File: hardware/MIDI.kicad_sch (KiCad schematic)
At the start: 0 parts

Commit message: feat: Created DIN5 MIDI Interface to Schematic
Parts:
- added D1, D3: LED, symbol Device:LED
- added D2: 1N4148, Diode_THT:D_DO-35_SOD27_P7.62mm_Horizontal, symbol Diode:1N4148
- added J2: DIN5_OUT, symbol Connector:DIN-5
- added J3: DIN5_IN, symbol Connector:DIN-5
- added R10, R11, R6, R7, R8, R9: R_US, symbol Device:R_US
- added U2: H11L1, symbol Isolator:H11L1
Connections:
- new net: D3.2 (A), R11.2
- new net: D2.1 (K), R10.2, U2.1
- new net: D2.2 (A), J3.5, U2.2
- new net: D1.2 (A), R8.2
- new net: J3.4, R10.1
- new net: J2.4, R9.2
- new net: J2.5, R7.1
- new net +5V: R11.1, R6.1, R8.1, R9.1, U2.6
- new net GND: J2.2, J3.2, U2.5
- new net RX: D3.1 (K), R6.2, U2.4
- new net TX: D1.1 (K), R7.2
- no-connect marks 0 -> 4
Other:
- note added: "Inspired by Adafruit MIDI Featherwing Schematic"

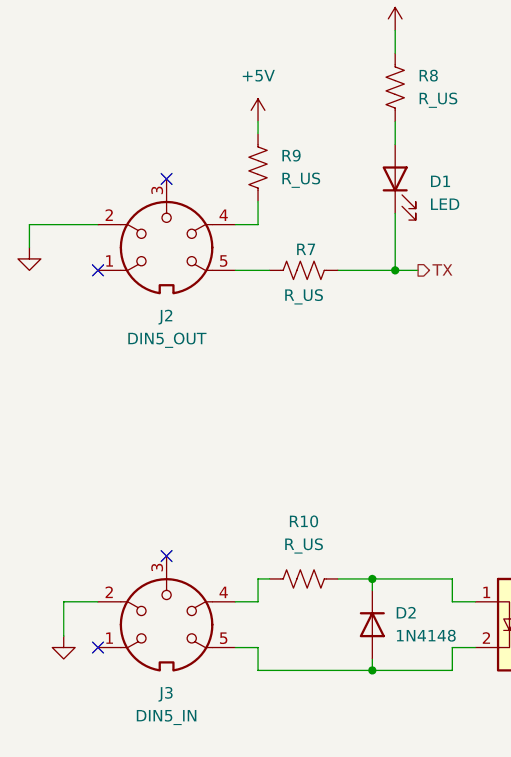
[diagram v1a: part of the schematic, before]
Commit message: feat: Created Button I2C Interfaces
For now, all we are using is generic 1x5 Connectors following the DFR Robot's RGB Button pinout https://wiki.dfrobot.com/SKU_DFR0991_Gravity_I2C_RGB_LED_Button_Module#target_9
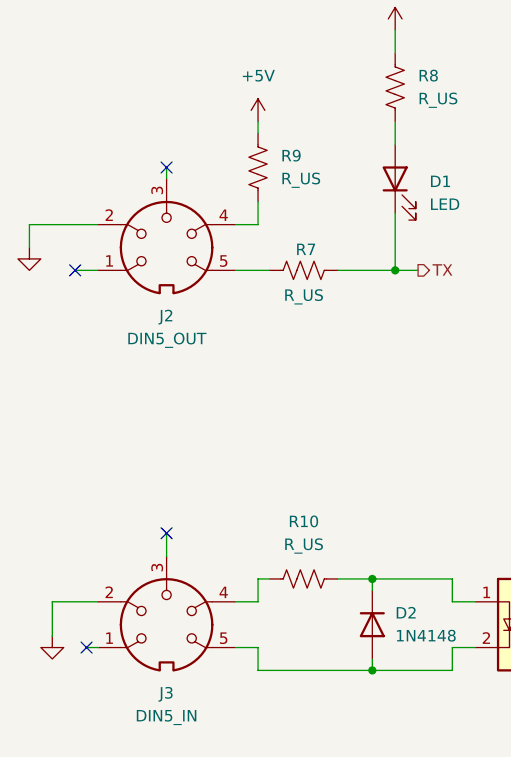
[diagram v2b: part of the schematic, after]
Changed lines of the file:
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@@
 	)
 	(no_connect
-		(at 63.5 52.07)
+		(at 63.5 50.8)
 	)
 	(no_connect
-		(at 55.88 104.14)
+		(at 54.61 104.14)
 	)
 	(no_connect
-		(at 63.5 93.98)
+		(at 63.5 91.44)
 	)
 	(no_connect
-		(at 55.88 62.23)
+		(at 53.34 62.23)
 	)
 	(wire
@@
 	(wire
 		(pts
+			(xy 53.34 62.23) (xy 55.88 62.23)
+		)
+		(stroke
+			(width 0)
+			(type default)
+		)
+	)
+	(wire
+		(pts
 			(xy 134.62 101.6) (xy 139.7 101.6)
 		)
@@
 	(wire
 		(pts
+			(xy 63.5 91.44) (xy 63.5 93.98)
+		)
+		(stroke
+			(width 0)
+			(type default)
+		)
+	)
+	(wire
+		(pts
 			(xy 134.62 76.2) (xy 134.62 78.74)
 		)
@@
 	(wire
 		(pts
-			(xy 52.07 99.06) (xy 55.88 99.06)
+			(xy 50.8 99.06) (xy 55.88 99.06)
 		)
 		(stroke
@@
 	(wire
 		(pts
+			(xy 63.5 50.8) (xy 63.5 52.07)
+		)
+		(stroke
+			(width 0)
+			(type default)
+		)
+	)
+	(wire
+		(pts
 			(xy 95.25 104.14) (xy 97.79 104.14)
 		)
@@
 	(wire
 		(pts
+			(xy 54.61 104.14) (xy 55.88 104.14)
+		)
+		(stroke
+			(width 0)
+			(type default)
+		)
+	)
+	(wire
+		(pts
 			(xy 73.66 96.52) (xy 74.93 96.52)
 		)
@@
 	(wire
 		(pts
-			(xy 52.07 99.06) (xy 52.07 102.87)
+			(xy 50.8 99.06) (xy 50.8 102.87)
 		)
 		(stroke
@@
 	(symbol
 		(lib_id "4ms_Power-symbol:GND")
-		(at 52.07 102.87 0)
+		(at 50.8 102.87 0)
 		(unit 1)
 		(exclude_from_sim no)
@@
 		(fields_autoplaced yes)
 		(property "Reference" "#PWR014"
-			(at 52.07 109.22 0)
+			(at 50.8 109.22 0)
 			(effects
 				(font
@@
 		)
 		(property "Value" "GND"
-			(at 52.07 107.95 0)
+			(at 50.8 107.95 0)
 			(effects
 				(font
@@
 		)
 		(property "Footprint" ""
-			(at 52.07 102.87 0)
+			(at 50.8 102.87 0)
 			(effects
 				(font
@@
 		)
 		(property "Datasheet" ""
-			(at 52.07 102.87 0)
+			(at 50.8 102.87 0)
 			(effects
 				(font
@@
 		)
 		(property "Description" ""
-			(at 52.07 102.87 0)
-			(effects
-				(font
+			(at 50.8 102.87 0)
+			(effects
+				(font

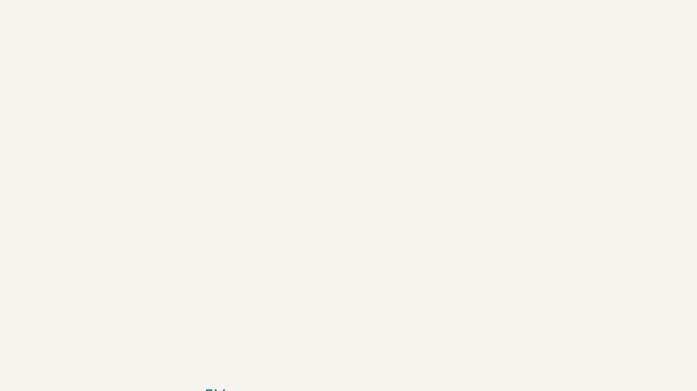
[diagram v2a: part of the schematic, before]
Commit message: feat: Added Footswitch Jack Conn for Tap Tempo
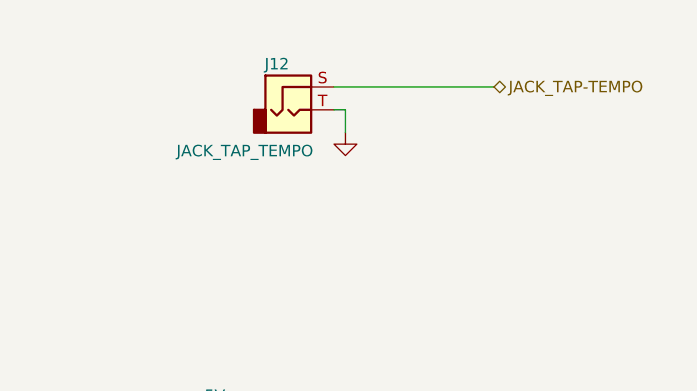
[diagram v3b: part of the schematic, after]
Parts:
- added J12: JACK_TAP_TEMPO, symbol Connector_Audio:AudioJack2
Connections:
- net GND: now also J12.T
- new net JACK_TAP-TEMPO: J12.S
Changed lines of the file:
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@@
+	(wire
+		(pts
+			(xy 148.59 39.37) (xy 149.86 39.37)
+		)
+		(stroke
+			(width 0)
+			(type default)
+		)
+	)
 	(wire
 		(pts
@@
 	(wire
 		(pts
+			(xy 148.59 36.83) (xy 166.37 36.83)
+		)
+		(stroke
+			(width 0)
+			(type default)
+		)
+	)
+	(wire
+		(pts
 			(xy 105.41 109.22) (xy 105.41 111.76)
+		)
+		(stroke
+			(width 0)
+			(type default)
+		)
+	)
+	(wire
+		(pts
+			(xy 149.86 39.37) (xy 149.86 41.91)
 		)
 		(stroke
@@
 		)
 	)
+	(hierarchical_label "JACK_TAP-TEMPO"
+		(shape bidirectional)
+		(at 166.37 36.83 0)
+		(effects
+			(font
+				(size 1.27 1.27)
+			)
+			(justify left)
+		)
+	)
 	(symbol
 		(lib_id "4ms_Power-symbol:+5V")
@@
 	)
 	(symbol
+		(lib_id "4ms_Power-symbol:GND")
+		(at 149.86 41.91 0)
+		(unit 1)
+		(exclude_from_sim no)
+		(in_bom yes)
+		(on_board yes)
+		(dnp no)
+		(fields_autoplaced yes)
+		(property "Reference" "#PWR039"
+			(at 149.86 48.26 0)
+			(effects
+				(font
+					(size 1.27 1.27)
+				)
+				(hide yes)
+			)
+		)
+		(property "Value" "GND"
+			(at 149.86 46.99 0)
+			(effects
+				(font
+					(size 1.27 1.27)
+				)
+				(hide yes)
+			)
+		)
+		(property "Footprint" ""
+			(at 149.86 41.91 0)
+			(effects
+				(font
+					(size 1.27 1.27)
+				)
+				(hide yes)
+			)
+		)
+		(property "Datasheet" ""
+			(at 149.86 41.91 0)
+			(effects
+				(font
+					(size 1.27 1.27)
+				)
+				(hide yes)
+			)
+		)
+		(property "Description" ""
+			(at 149.86 41.91 0)
+			(effects
+				(font
+					(size 1.27 1.27)
+				)
+				(hide yes)
+			)
+		)
+		(pin "1"
+		)
+		(instances
+			(project "10032025_01_[HWE] Simple Transport Midi Controller"
+				(path "/4f4cdf46-015d-4b38-9cc1-de7a767260f6/1cf1d960-9678-42ca-8223-9c2d1c27161c"
+					(reference "#PWR039")
+					(unit 1)
+				)
+			)
+		)
+	)
+	(symbol
 		(lib_id "Device:R_US")
 		(at 73.66 50.8 0)
@@
 					(unit 1)
 				)
+			)
+		)
+	)
+	(symbol
+		(lib_id "Connector_Audio:AudioJack2")
+		(at 143.51 39.37 0)
+		(unit 1)
+		(exclude_from_sim no)
+		(in_bom yes)
+		(on_board yes)
+		(dnp no)
+		(property "Reference" "J12"
+			(at 142.24 34.29 0)
+			(effects
+				(font
+					(size 1.27 1.27)
+				)
+			)
+		)
+		(property "Value" "JACK_TAP_TEMPO"
+			(at 138.684 43.942 0)
+			(effects
+				(font
+					(size 1.27 1.27)
+				)
+			)
+		)
+		(property "Footprint" ""
+			(at 143.51 39.37 0)
+			(effects
+				(font
+					(size 1.27 1.27)
+				)
+				(hide yes)
+			)
+		)
+		(property "Datasheet" "~"
+			(at 143.51 39.37 0)
+			(effects
+				(font
+					(size 1.27 1.27)
+				)
+				(hide yes)
+			)
+		)
+		(property "Description" "Audio Jack, 2 Poles (Mono / TS)"
+			(at 143.51 39.37 0)
+			(effects
+				(font
+					(size 1.27 1.27)
+				)
+				(hide yes)
+			)
+		)
+		(pin "S"
+		)
+		(pin "T"
+		)
+		(instances
+			(project ""
+				(path "/4f4cdf46-015d-4b38-9cc1-de7a767260f6/1cf1d960-9678-42ca-8223-9c2d1c27161c"
+					(reference "J12")
+					(unit 1)
+				)

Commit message: feat![HWE]: Changed MCU to Adafruit ESP32-S3
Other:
- company: (none) -> Madueke Systems and Technologies
- title: (none) -> Simple Midi Transport Controller
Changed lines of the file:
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@@
 	(generator_version "9.0")
 	(paper "A4")
+	(title_block
+		(title "Simple Midi Transport Controller")
+		(date "2026-04-06")
+		(rev "1")
+		(company "Madueke Systems and Technologies")
+		(comment 1 "Used the combination of the Adafruit Feather ESP32-V2 Dev Board and the SX1509 IO expander")
+	)
 	(text "Inspired by Adafruit MIDI Featherwing Schematic\n"
 		(exclude_from_sim no)
